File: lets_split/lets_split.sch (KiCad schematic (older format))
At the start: 59 parts, among them J1 Speaker, P1 USB-rewire, P2 USB_OTG, P3 WS2812-Strip, P4 TRRS jack, SW1 SW_PUSH, SW10 SW_PUSH, SW11 SW_PUSH, SW12 SW_PUSH, SW13 SW_PUSH, SW14 SW_PUSH, SW15 SW_PUSH, SW16 SW_PUSH, SW17 SW_PUSH, SW18 SW_PUSH, SW19 SW_PUSH, SW2 SW_PUSH, SW20 SW_PUSH, SW21 SW_PUSH, SW22 SW_PUSH, SW23 SW_PUSH, SW24 SW_PUSH, SW3 SW_PUSH, SW4 SW_PUSH, SW5 SW_PUSH, SW6 SW_PUSH, SW7 SW_PUSH, SW8 SW_PUSH, SW9 SW_PUSH, U1 ArduinoProMicro

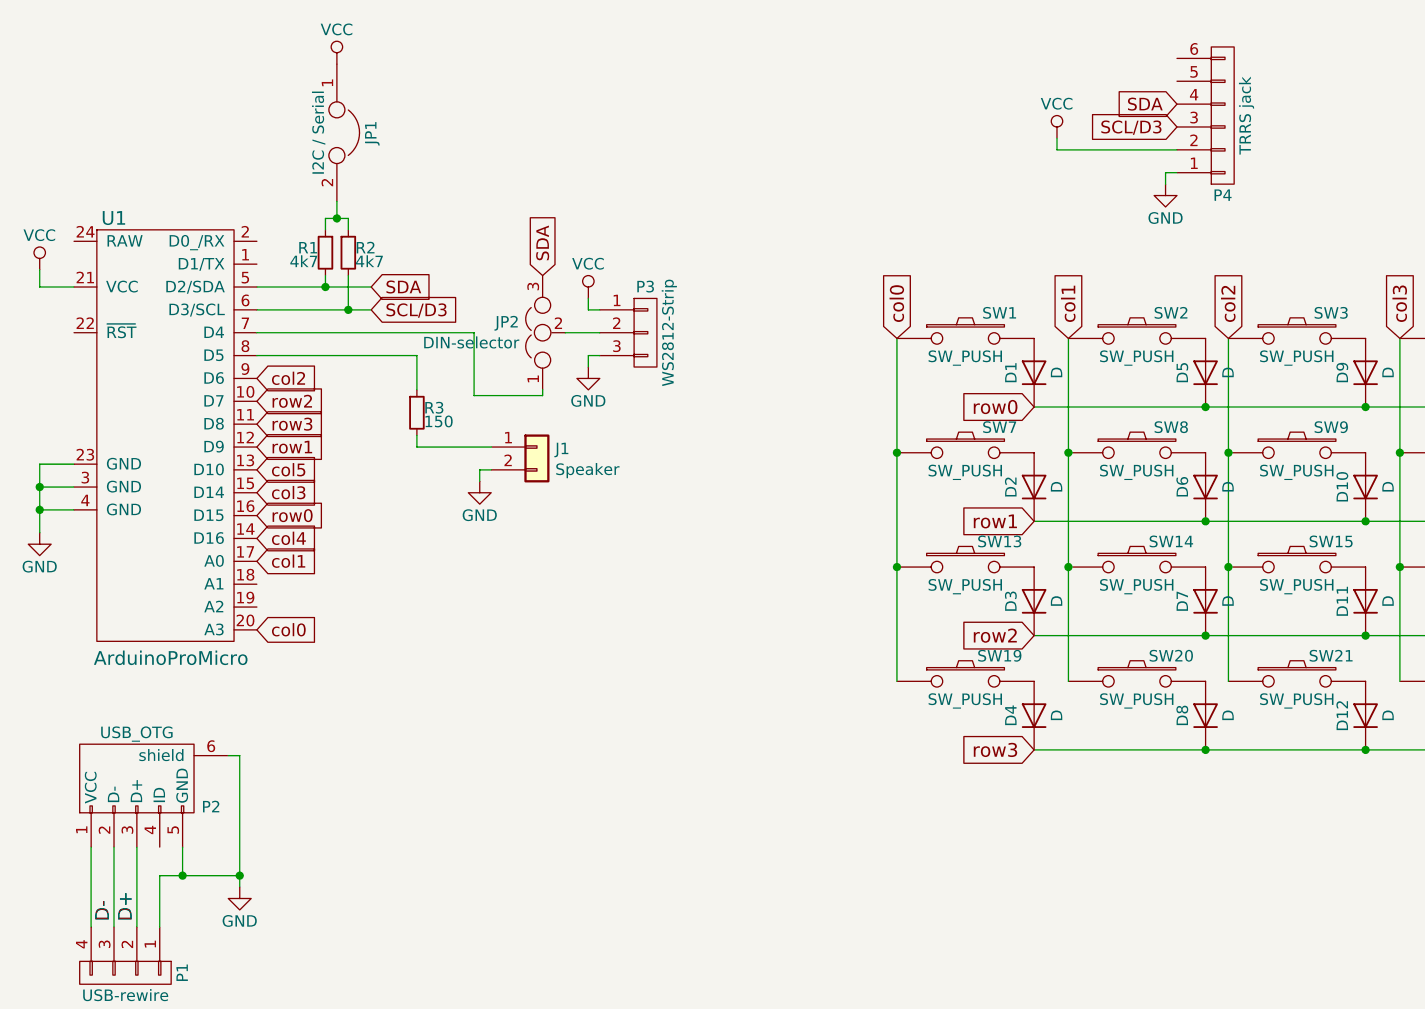
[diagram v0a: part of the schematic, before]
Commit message: Changed footpring designations for possible PCBA in the future
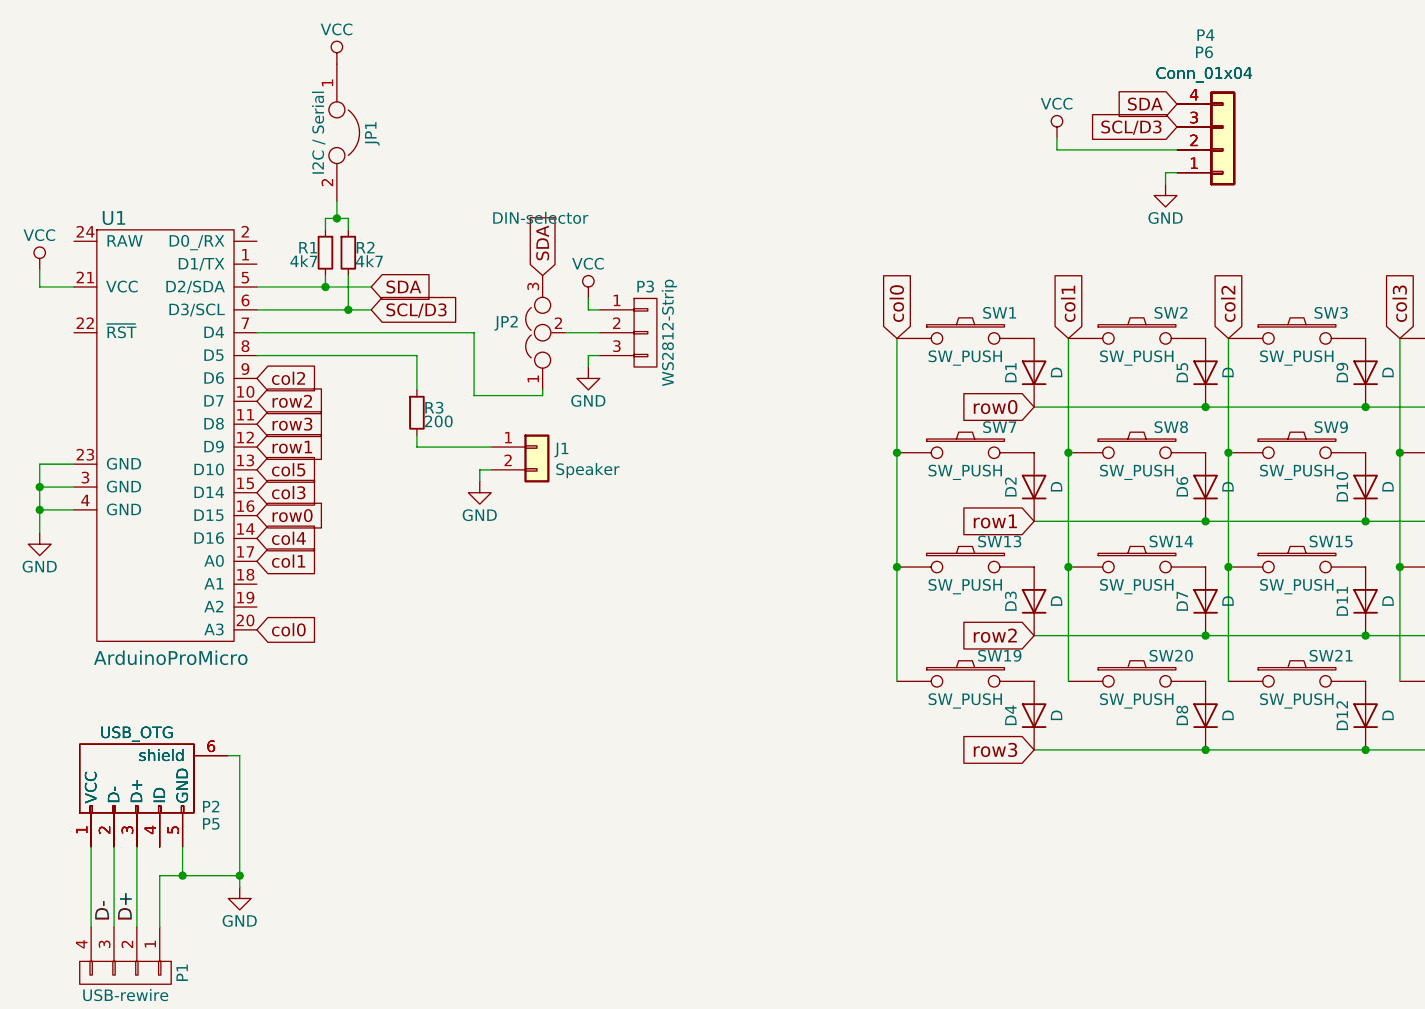
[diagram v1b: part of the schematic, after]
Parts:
- removed P4: TRRS jack, Connectors:SJ-4351X-SMT, symbol CONN_01X06
- added P4, P6: Conn_01x04, Connectors:SJ-4351X-SMT, symbol Conn_01x04
- added P5: USB_OTG, Connectors:USB-Mini-B-SMD, symbol USB_OTG-RESCUE-lets_split
- R3: value 150 -> 200
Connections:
- net D+: now also P5.3 (D+)
- net D-: now also P5.2 (D-)
- net GND: now also P4.1 (Pin_1), P5.5 (GND), P5.6 (shield), P6.1 (Pin_1)
- net SCL/D3: now also P4.3 (Pin_3), P6.3 (Pin_3)
- net SDA: now also P4.4 (Pin_4), P6.4 (Pin_4)
- net VCC: now also P4.2 (Pin_2), P6.2 (Pin_2)
- net at P1.4 (P4), P2.1 (VCC): now also P5.1 (VCC)
- net at P2.4 (ID): now also P5.4 (ID)
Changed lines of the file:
@@
 	3800 2275 3850 2275
-$Comp
-L CONN_01X06 P4
-U 1 1 59DEE7A5
-P 6575 1225
-F 0 "P4" H 6575 1575 50  0000 C CNN
-F 1 "TRRS jack" V 6675 1225 50  0000 C CNN
-F 2 "Connectors:SJ-4351X-SMT" H 6575 1225 50  0001 C CNN
-F 3 "" H 6575 1225 50  0000 C CNN
-	1    6575 1225
-	1    0    0    1
-$EndComp
 $Comp
 L Conn_01x02 J1
@@
 P 3050 2525
 F 0 "R3" H 3080 2545 50  0000 L CNN
-F 1 "150" H 3080 2485 50  0000 L CNN
+F 1 "200" H 3080 2485 50  0000 L CNN
 F 2 "Resistors_SMD:R_0603_HandSoldering" H 3050 2525 50  0001 C CNN
 F 3 "" H 3050 2525 50  0000 C CNN
@@
 P 3600 2175
 F 0 "JP2" V 3646 2277 50  0000 L CNN
-F 1 "DIN-selector" V 3555 2277 50  0000 L CNN
+F 1 "DIN-selector" V 4100 1975 50  0000 L CNN
 F 2 "Jumpers:Solder-jumper-12NC-23NO" H 3600 2175 50  0001 C CNN
 F 3 "" H 3600 2175 50  0001 C CNN
@@
 Text GLabel 3600 1925 1    55   Input ~ 0
 SDA
+$Comp
+L USB_OTG-RESCUE-lets_split P5
+U 1 1 59F15E46
+P 1825 4125
+F 0 "P5" H 2150 3925 50  0000 C CNN
+F 1 "USB_OTG" H 1825 4325 50  0000 C CNN
+F 2 "Connectors:USB-Mini-B-SMD" V 1775 4025 50  0001 C CNN
+F 3 "" V 1775 4025 50  0000 C CNN
+	1    1825 4125
+	1    0    0    -1
+$EndComp
+$Comp
+L Conn_01x04 P4
+U 1 1 59F16640
+P 6575 1375
+F 0 "P4" H 6500 875 50  0000 C CNN
+F 1 "Conn_01x04" H 6494 1041 50  0000 C CNN
+F 2 "Connectors:SJ-4351X-SMT" H 6575 1375 50  0001 C CNN
+F 3 "" H 6575 1375 50  0001 C CNN
+	1    6575 1375
+	1    0    0    1
+$EndComp
+$Comp
+L Conn_01x04 P6
+U 1 1 59F174F6
+P 6575 1375
+F 0 "P6" H 6494 950 50  0000 C CNN
+F 1 "Conn_01x04" H 6494 1041 50  0000 C CNN
+F 2 "Connectors:SJ-4351X-SMT" H 6575 1375 50  0001 C CNN
+F 3 "" H 6575 1375 50  0001 C CNN
+	1    6575 1375
+	1    0    0    1
+$EndComp
 $EndSCHEMATC

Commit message: Vitamins included "done"
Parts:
- removed JP2: DIN-selector, Jumpers:Solder-jumper-12NC-23NO, symbol Jumper_NC_Dual
- removed P1: USB-rewire, Pin_Headers:Pin_Header_Straight_1x04_Pitch2.00mm, symbol CONN_01X04
- removed P5: USB_OTG, Connectors:USB-Mini-B-SMD, symbol USB_OTG-RESCUE-lets_split
- removed P6: Conn_01x04, Connectors:SJ-4351X-SMT, symbol Conn_01x04
- removed U1: ArduinoProMicro, plug-in-modules:ArduinoProMicro, symbol ArduinoProMicro
- added C1, C4: 1uF, SeeedOPL-Capacitor-2016:C0603, symbol C_Small
- added C2, C3: 8pF, SeeedOPL-Capacitor-2016:C0402, symbol C_Small
- added J2: RST, Pin_Headers:Pin_Header_Straight_1x02_Pitch2.54mm, symbol Conn_01x02
- added J3: ISP, Jlink:J-link-needle-6pin, symbol Conn_02x03_Odd_Even
- added JP2: I2C pullup, Jumpers:Solder-jumper-NO, symbol JUMPER
- added P1: WS2812>, Wirepads:SMD_PAD_1x03_Pitch2.54mm, symbol CONN_01X03
- added R4, R5: 22R, Resistors_SMD:R_0603_HandSoldering, symbol R_Small
- added R6: 4k7, Resistors_SMD:R_0603_HandSoldering, symbol R_Small
- added U1: ATMega32U4, SeeedOPL-IC-2016:QFN44G-0.5-7X7MM, symbol ATMega32U4
- added Y1: Crystal, SeeedOPL-Crystal Oscillator-2016:X2-SMD-3.2X1.5X0.55MM, symbol Crystal
- D1, D10, D11, D12, D13, D14, D15, D16, D17, D18, D19, D2, D20, D21, D22, D23, D24, D3, D4, D5, D6, D7, D8, D9: footprint Diodes_ThroughHole:D_DO-41_SOD81_P7.62mm_Horizontal -> SeeedOPL-Diode-2016:DO-214AC
- JP1: value I2C / Serial -> I2C pullup
- P3: value WS2812-Strip -> >WS2812
- R1, R2: footprint Resistors_ThroughHole:R_Axial_DIN0207_L6.3mm_D2.5mm_P10.16mm_Horizontal -> Resistors_SMD:R_0603_HandSoldering
- SW1, SW10, SW11, SW12, SW13, SW14, SW15, SW16, SW17, SW18, SW19, SW2, SW20, SW21, SW22, SW23, SW24, SW3, SW4, SW5, SW6, SW7, SW8, SW9: footprint CherryMX:Kailh-socket-mirrorable -> CherryMX:Kailh-socket
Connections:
- net VCC is gone; now on net VBUS: JP1.1, P3.1 (P1), P4.2 (Pin_2)
- net D+: now also R5.2, U1.4 (D+); no longer P2.3 (D+)
- net D-: now also R4.2, U1.3 (D-); no longer P2.2 (D-)
- net GND: now also C1.2, C2.2, C3.2, C4.2, J2.1 (Pin_1), J3.6 (Pin_6), P1.3 (P3), U1.15 (GND), U1.23 (GND), U1.35 (GND), U1.43 (GND), U1.5 (UGND), U1.TAB (GND)
- net SCL/D3: now also U1.18 (~~(INT0/SCL)PD0)
- net SDA: now also P1.2 (P2), U1.19 ((INT1/SDA)PD1)
- net col0: now also U1.40 ((A1)PF1)
- net col1: now also U1.39 ((A4)PF4)
- net col2: now also U1.33 (PE2)
- net col3: now also U1.30 (~~(A13)PB6)
- net col4: now also U1.27 (~~(ADC10)PD7)
- net col5: now also U1.26 (~~(ADC9)PD6)
- net row0: now also U1.38 ((A5)PF5)
- net row1: now also U1.37 ((A6)PF6)
- net row2: now also U1.32 (~~PC7)
- net row3: now also U1.36 ((A7)PF7)
- net buzz: now reaches R3.1
- net buzz: now also U1.31 (~~PC6)
- net at JP1.2, R1.1: no longer R2.1
- net VBUS: now reaches P2.1 (VCC)
- net VBUS: now also C1.1, J3.2 (Pin_2), JP2.1, P1.1 (P1), R6.2, U1.14 (VCC), U1.2 (UVCC), U1.24 (AVCC), U1.34 (VCC), U1.44 (AVCC), U1.7 (VBUS)
- net WD2812-in: now reaches P3.2 (P2)
- net WD2812-in: now also U1.41 ((A0)PF0)
- new net: JP2.2, R2.1
- new net: P2.2 (D-), R4.1
- new net: P2.3 (D+), R5.1
- new net: C3.1, U1.16 (XTAL2), Y1.2
- new net: C2.1, U1.17 (XTAL1), Y1.1
- new net: C4.1, U1.6 (UCap)
- new net MISO: J3.1 (Pin_1), U1.11 ((MISO)PB3)
- new net MOSI: J3.4 (Pin_4), U1.10 ((MOSI)PB2)
- new net SCK: J3.3 (Pin_3), U1.9 ((SCK)PB1)
- new net ~RESET: J2.2 (Pin_2), J3.5 (Pin_5), R6.1, U1.13 (~RESET~)
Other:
- moved on the sheet: D1, D10, D11, D12, D13, D14, D15, D16, D17, D18, D19, D2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
